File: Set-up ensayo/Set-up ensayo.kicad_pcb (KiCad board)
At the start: 2 copper layers, 17 parts, among them J1 Conn_Coaxial, J2 DB9_Female_MountingHoles

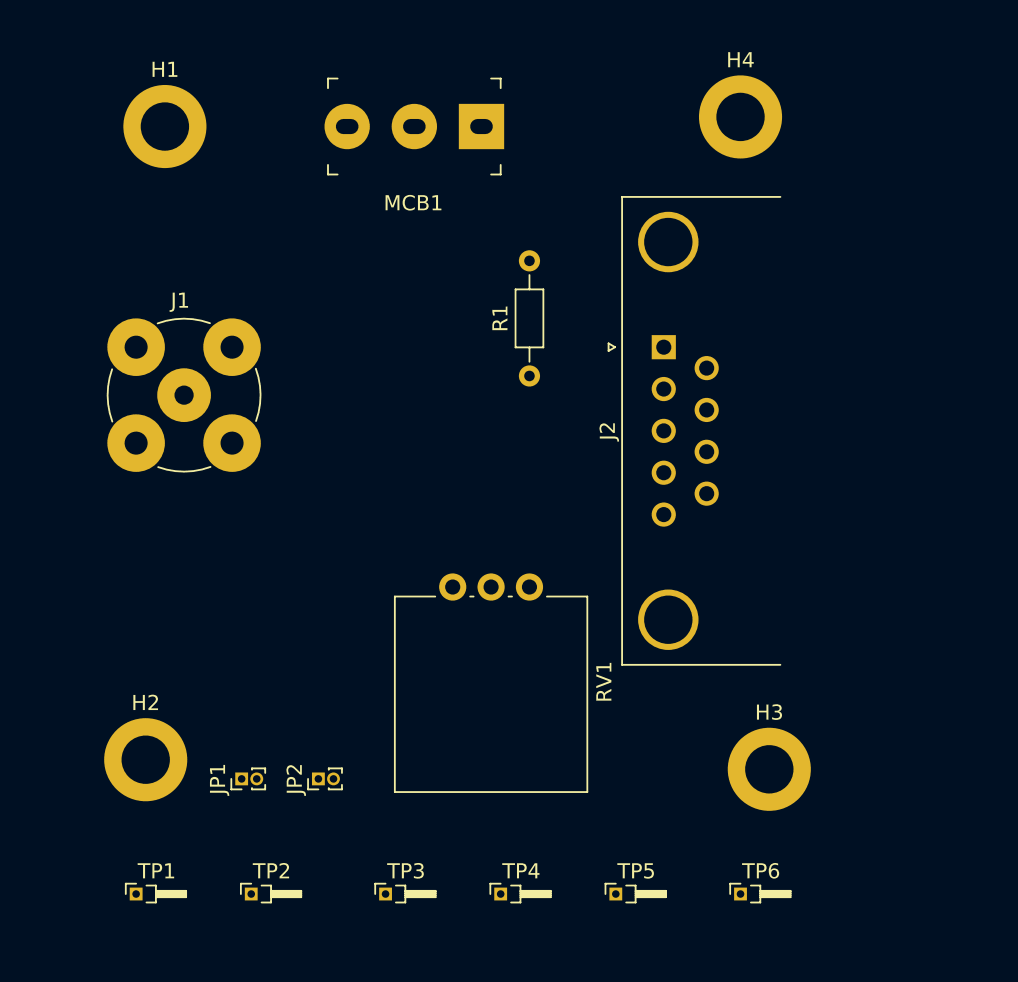
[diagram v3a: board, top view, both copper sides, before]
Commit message: Empecé con el 2do paso del proceso de diseño de PCB, definí el tamaño del PCB 60x60mm2, queda pendiente hacer los bordes redondeados, ja
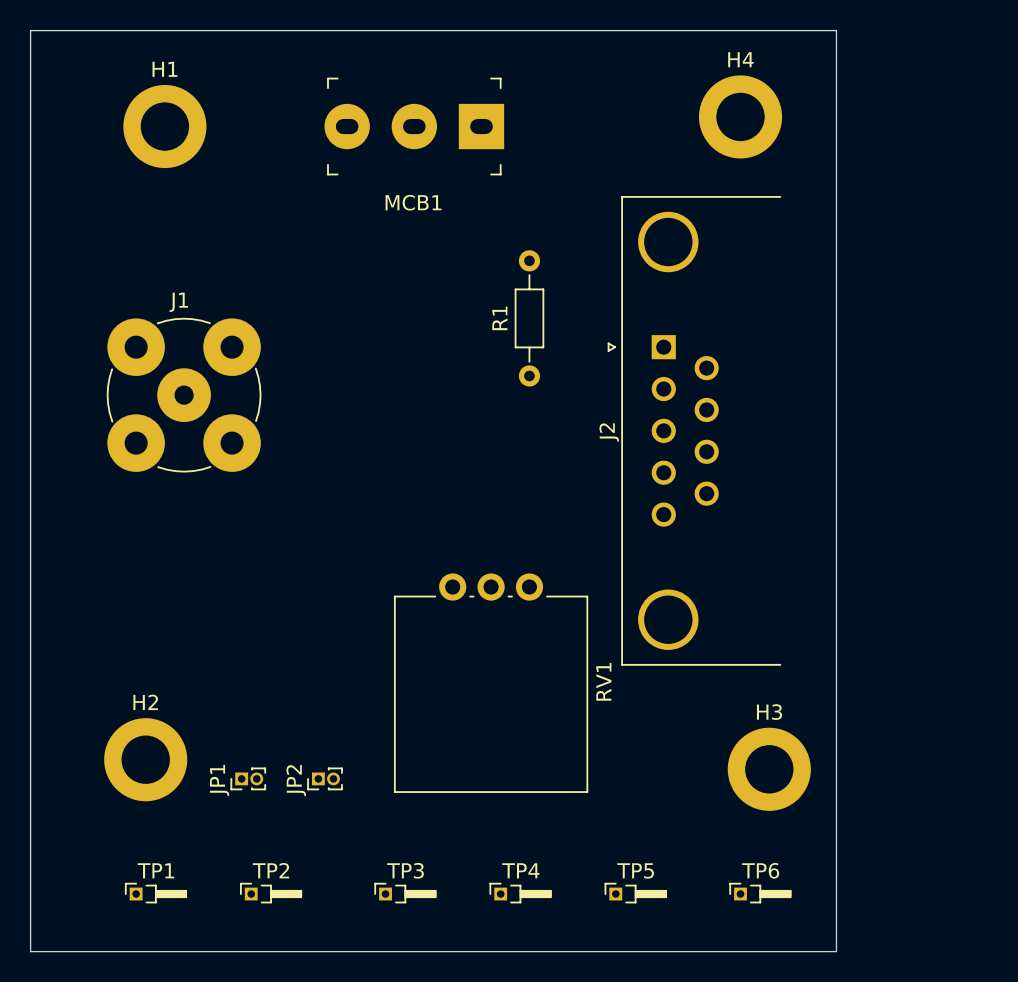
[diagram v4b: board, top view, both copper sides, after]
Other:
- board outline added: 53.3 x 61 mm
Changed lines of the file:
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@@
   (general
     (thickness 1.6)
-    (drawings 0)
+    (drawings 4)
     (tracks 0)
     (zones 0)
@@
     )
   )
+  (gr_line (start 149.86 74.93) (end 96.52 74.93) (layer Edge.Cuts) (width 0.05))
+  (gr_line (start 149.86 135.89) (end 149.86 74.93) (layer Edge.Cuts) (width 0.05))
+  (gr_line (start 96.52 135.89) (end 149.86 135.89) (layer Edge.Cuts) (width 0.05))
+  (gr_line (start 96.52 74.93) (end 96.52 135.89) (layer Edge.Cuts) (width 0.05))
 )
